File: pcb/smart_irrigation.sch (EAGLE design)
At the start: 22 parts, among them IC1 7805DT, IC2 7833DT, IC3 TMP36, J1 1X2-3.5MM, Q2 32.768

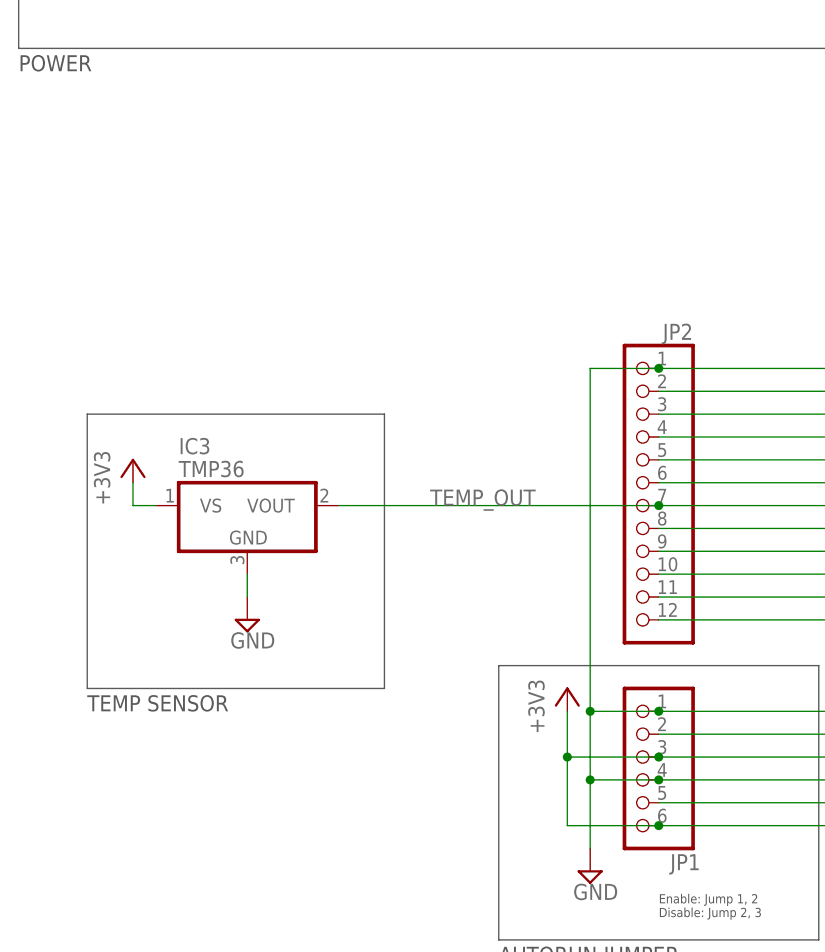
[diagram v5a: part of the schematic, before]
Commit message: PCB: Add soil moisture sensor
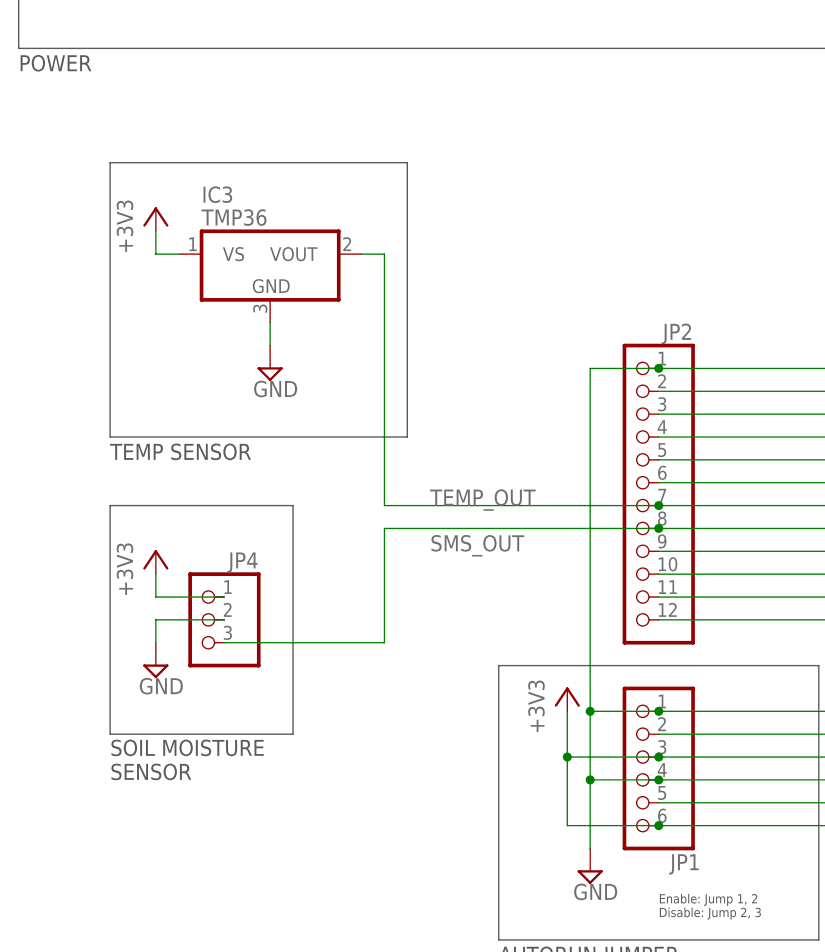
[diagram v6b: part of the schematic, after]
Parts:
- added JP4: (no value), pinhead:PINHD-1X3
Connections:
- removed net N$10: JP2.8, U$1.SIO_2/AIN
- new net SMS_OUT: JP2.8, JP4.3, U$1.SIO_2/AIN
- net +3V3: now also JP4.1
- net GND: now also JP4.2
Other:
- note added: "SOIL MOISTURE SENSOR"
- moved on the sheet: IC3
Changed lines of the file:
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@@
 <part name="+3V5" library="supply1" deviceset="+3V3" device=""/>
 <part name="SUPPLY18" library="supply2" deviceset="GND" device=""/>
+<part name="JP4" library="pinhead" deviceset="PINHD-1X3" device=""/>
+<part name="+3V6" library="supply1" deviceset="+3V3" device=""/>
+<part name="SUPPLY21" library="supply2" deviceset="GND" device=""/>
 </parts>
 <sheets>
@@
 <wire x1="210.82" y1="121.92" x2="210.82" y2="71.12" width="0.1524" layer="97"/>
 <text x="210.82" y="68.58" size="1.778" layer="97">RTC</text>
-<wire x1="12.7" y1="127" x2="45.72" y2="127" width="0.1524" layer="97"/>
-<wire x1="45.72" y1="127" x2="45.72" y2="96.52" width="0.1524" layer="97"/>
-<wire x1="45.72" y1="96.52" x2="12.7" y2="96.52" width="0.1524" layer="97"/>
-<wire x1="12.7" y1="96.52" x2="12.7" y2="127" width="0.1524" layer="97"/>
-<text x="12.7" y="93.98" size="1.778" layer="97">TEMP SENSOR</text>
+<wire x1="15.24" y1="154.94" x2="48.26" y2="154.94" width="0.1524" layer="97"/>
+<wire x1="48.26" y1="154.94" x2="48.26" y2="124.46" width="0.1524" layer="97"/>
+<wire x1="48.26" y1="124.46" x2="15.24" y2="124.46" width="0.1524" layer="97"/>
+<wire x1="15.24" y1="124.46" x2="15.24" y2="154.94" width="0.1524" layer="97"/>
+<text x="15.24" y="121.92" size="1.778" layer="97">TEMP SENSOR</text>
+<wire x1="15.24" y1="116.84" x2="35.56" y2="116.84" width="0.1524" layer="97"/>
+<wire x1="35.56" y1="116.84" x2="35.56" y2="91.44" width="0.1524" layer="97"/>
+<wire x1="35.56" y1="91.44" x2="15.24" y2="91.44" width="0.1524" layer="97"/>
+<wire x1="15.24" y1="91.44" x2="15.24" y2="116.84" width="0.1524" layer="97"/>
+<text x="15.24" y="86.36" size="1.778" layer="97">SOIL MOISTURE
+SENSOR</text>
 </plain>
 <instances>
@@
 <instance part="+3V3" gate="G$1" x="190.5" y="119.38"/>
 <instance part="+3V4" gate="G$1" x="198.12" y="119.38"/>
-<instance part="IC3" gate="A1" x="30.48" y="116.84"/>
-<instance part="+3V5" gate="G$1" x="17.78" y="121.92"/>
-<instance part="SUPPLY18" gate="GND" x="30.48" y="104.14"/>
+<instance part="IC3" gate="A1" x="33.02" y="144.78"/>
+<instance part="+3V5" gate="G$1" x="20.32" y="149.86"/>
+<instance part="SUPPLY18" gate="GND" x="33.02" y="132.08"/>
+<instance part="JP4" gate="A" x="25.4" y="104.14" rot="MR0"/>
+<instance part="+3V6" gate="G$1" x="20.32" y="111.76"/>
+<instance part="SUPPLY21" gate="GND" x="20.32" y="99.06"/>
 </instances>
 <busses>
@@
 <pinref part="IC3" gate="A1" pin="GND"/>
 <pinref part="SUPPLY18" gate="GND" pin="GND"/>
-<wire x1="30.48" y1="109.22" x2="30.48" y2="106.68" width="0.1524" layer="91"/>
+<wire x1="33.02" y1="137.16" x2="33.02" y2="134.62" width="0.1524" layer="91"/>
+</segment>
+<segment>
+<pinref part="SUPPLY21" gate="GND" pin="GND"/>
+<wire x1="20.32" y1="101.6" x2="20.32" y2="104.14" width="0.1524" layer="91"/>
+<pinref part="JP4" gate="A" pin="2"/>
+<wire x1="20.32" y1="104.14" x2="27.94" y2="104.14" width="0.1524" layer="91"/>
 </segment>
 </net>
@@
 <segment>
 <pinref part="+3V5" gate="G$1" pin="+3V3"/>
-<wire x1="17.78" y1="119.38" x2="17.78" y2="116.84" width="0.1524" layer="91"/>
+<wire x1="20.32" y1="147.32" x2="20.32" y2="144.78" width="0.1524" layer="91"/>
 <pinref part="IC3" gate="A1" pin="VS"/>
-<wire x1="17.78" y1="116.84" x2="20.32" y2="116.84" width="0.1524" layer="91"/>
+<wire x1="20.32" y1="144.78" x2="22.86" y2="144.78" width="0.1524" layer="91"/>
+</segment>
+<segment>
+<pinref part="+3V6" gate="G$1" pin="+3V3"/>
+<wire x1="20.32" y1="109.22" x2="20.32" y2="106.68" width="0.1524" layer="91"/>
+<pinref part="JP4" gate="A" pin="1"/>
+<wire x1="20.32" y1="106.68" x2="27.94" y2="106.68" width="0.1524" layer="91"/>
 </segment>
 </net>
@@
 <pinref part="U$1" gate="G$1" pin="SIO_1/AIN"/>
 <wire x1="76.2" y1="116.84" x2="99.06" y2="116.84" width="0.1524" layer="91"/>
+<label x="50.8" y="116.84" size="1.778" layer="95"/>
 <pinref part="IC3" gate="A1" pin="VOUT"/>
-<wire x1="40.64" y1="116.84" x2="76.2" y2="116.84" width="0.1524" layer="91"/>
+<wire x1="43.18" y1="144.78" x2="45.72" y2="144.78" width="0.1524" layer="91"/>
+<wire x1="45.72" y1="144.78" x2="45.72" y2="116.84" width="0.1524" layer="91"/>
+<wire x1="45.72" y1="116.84" x2="76.2" y2="116.84" width="0.1524" layer="91"/>
 <junction x="76.2" y="116.84"/>
-<label x="50.8" y="116.84" size="1.778" layer="95"/>
-</segment>
-</net>
-<net name="N$10" class="0">
+</segment>
+</net>
+<net name="SMS_OUT" class="0">
 <segment>
 <pinref part="U$1" gate="G$1" pin="SIO_2/AIN"/>
 <pinref part="JP2" gate="G$1" pin="8"/>
 <wire x1="99.06" y1="114.3" x2="76.2" y2="114.3" width="0.1524" layer="91"/>
-</segment>
-</net>
+<pinref part="JP4" gate="A" pin="3"/>
+<wire x1="27.94" y1="101.6" x2="45.72" y2="101.6" width="0.1524" layer="91"/>
+<wire x1="45.72" y1="101.6" x2="45.72" y2="114.3" width="0.1524" layer="91"/>
+<wire x1="45.72" y1="114.3" x2="76.2" y2="114.3" width="0.1524" layer="91"/>
+<junction x="76.2" y="114.3"/>
+<label x="50.8" y="111.76" size="1.778" layer="95"/>
+</segment>
+</net>

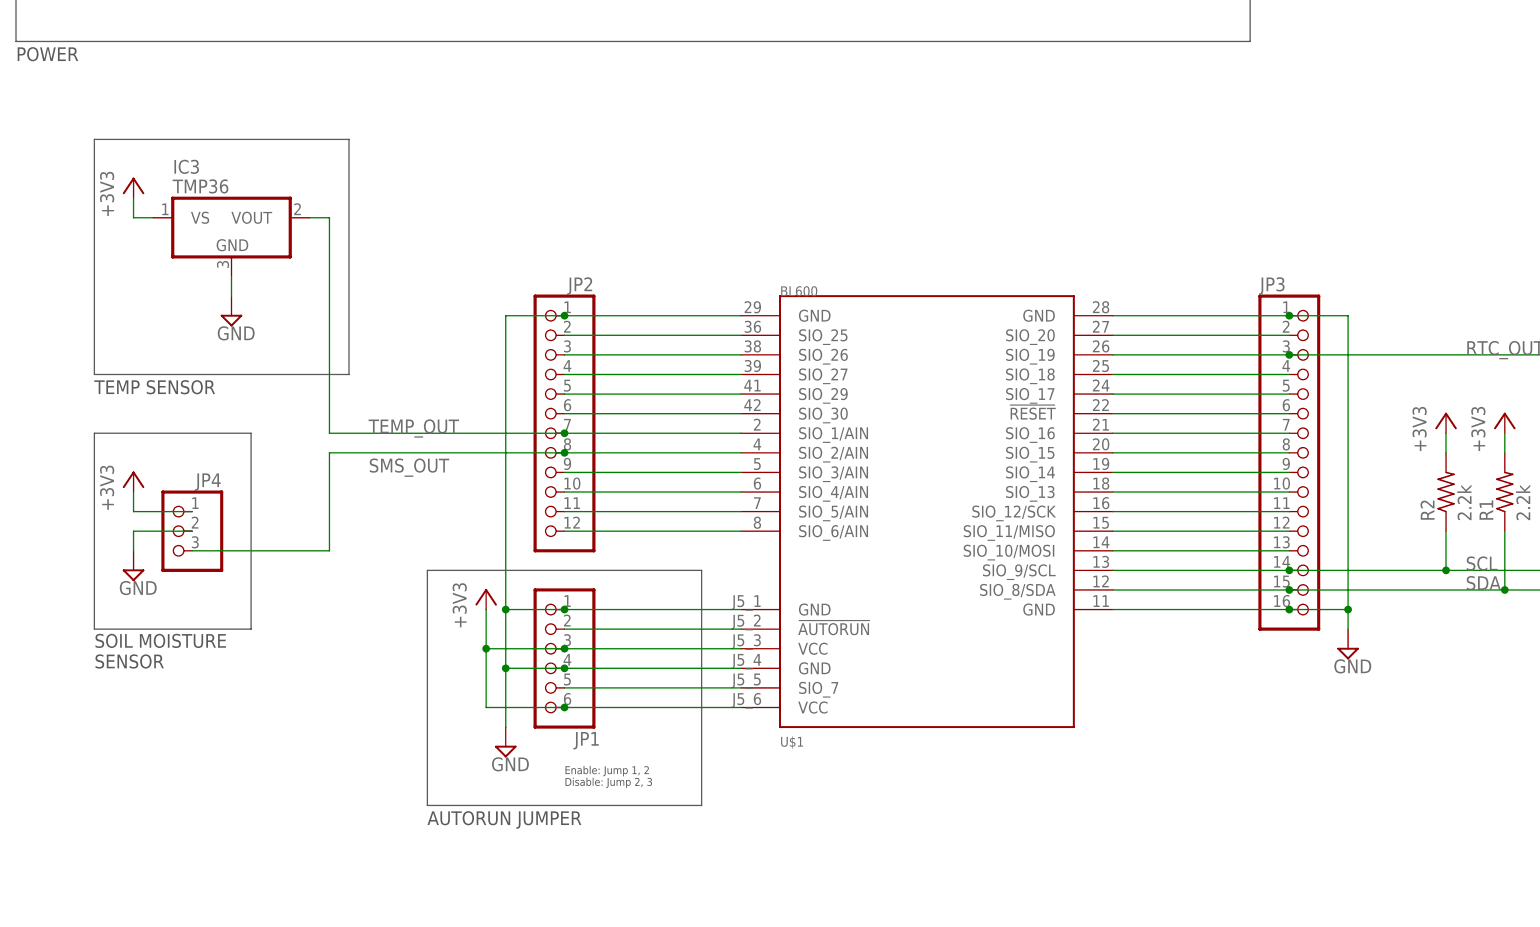
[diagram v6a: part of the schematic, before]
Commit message: PCB: Add raindrop sensor
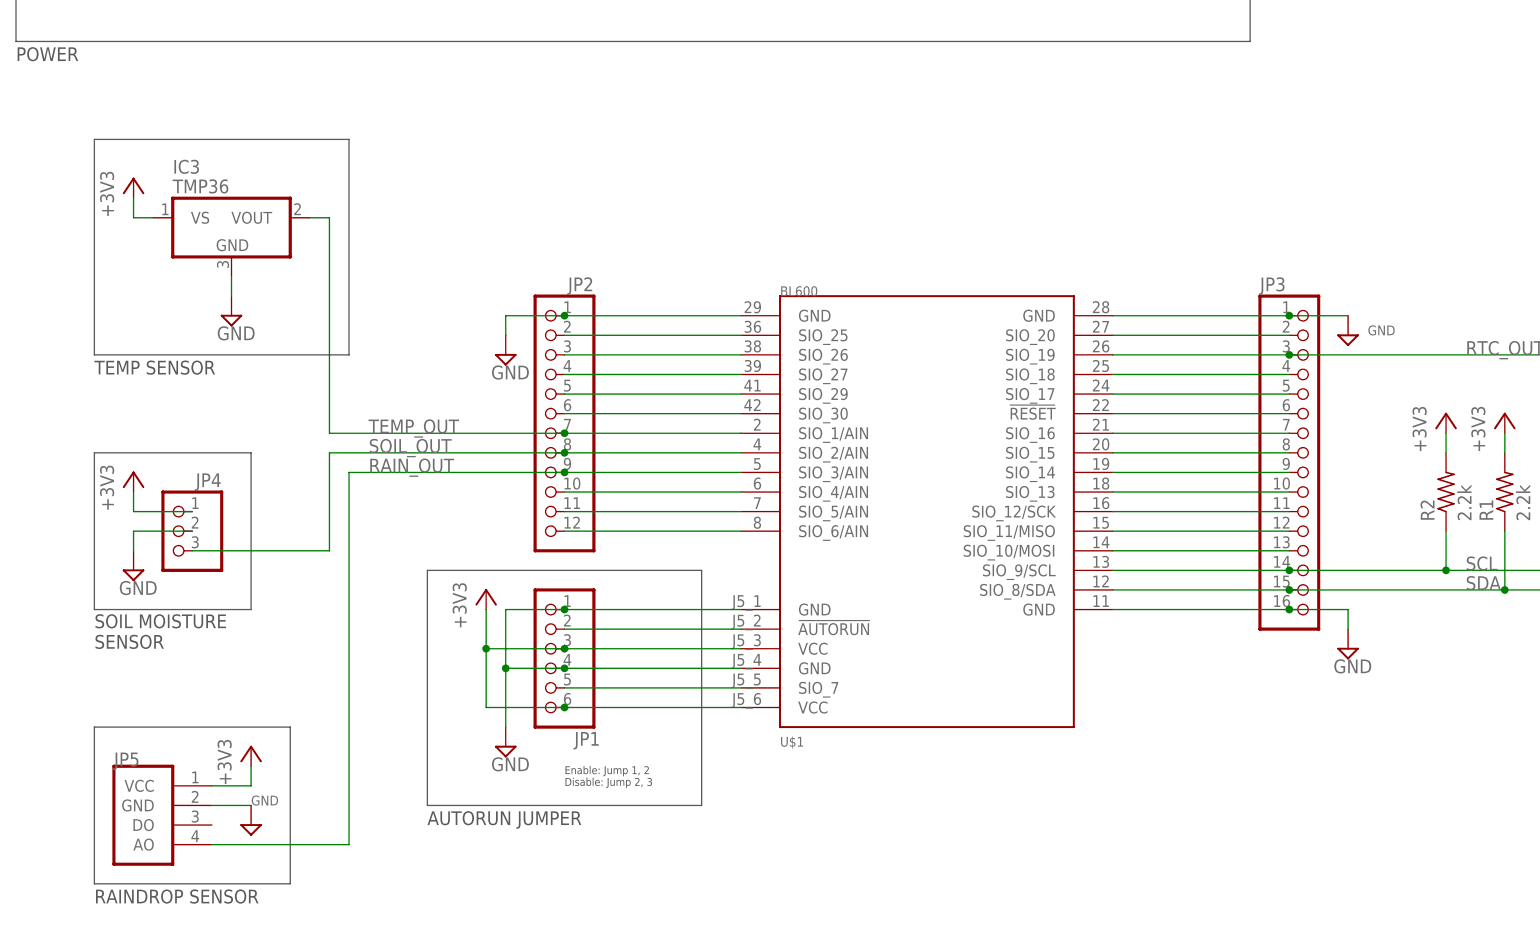
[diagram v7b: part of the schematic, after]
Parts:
- added JP5: (no value), smart_irrigation:RAINDROP
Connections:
- net N$1 renamed NAUTORUN
- net SMS_OUT renamed SOIL_OUT
- removed net N$11: JP2.9, U$1.SIO_3/AIN
- new net RAIN_OUT: JP2.9, JP5.AO, U$1.SIO_3/AIN
- net +3V3: now also JP5.VCC
- net GND: now also JP5.GND
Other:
- note added: "RAINDROP SENSOR"
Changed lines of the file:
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@@
 <part name="+3V6" library="supply1" deviceset="+3V3" device=""/>
 <part name="SUPPLY21" library="supply2" deviceset="GND" device=""/>
+<part name="JP5" library="smart_irrigation" deviceset="RAINDROP" device=""/>
+<part name="+3V7" library="supply1" deviceset="+3V3" device=""/>
+<part name="SUPPLY22" library="supply2" deviceset="GND" device=""/>
+<part name="SUPPLY23" library="supply2" deviceset="GND" device=""/>
+<part name="SUPPLY24" library="supply2" deviceset="GND" device=""/>
 </parts>
 <sheets>
@@
 <text x="210.82" y="68.58" size="1.778" layer="97">RTC</text>
 <wire x1="15.24" y1="154.94" x2="48.26" y2="154.94" width="0.1524" layer="97"/>
-<wire x1="48.26" y1="154.94" x2="48.26" y2="124.46" width="0.1524" layer="97"/>
-<wire x1="48.26" y1="124.46" x2="15.24" y2="124.46" width="0.1524" layer="97"/>
-<wire x1="15.24" y1="124.46" x2="15.24" y2="154.94" width="0.1524" layer="97"/>
-<text x="15.24" y="121.92" size="1.778" layer="97">TEMP SENSOR</text>
-<wire x1="15.24" y1="116.84" x2="35.56" y2="116.84" width="0.1524" layer="97"/>
-<wire x1="35.56" y1="116.84" x2="35.56" y2="91.44" width="0.1524" layer="97"/>
-<wire x1="35.56" y1="91.44" x2="15.24" y2="91.44" width="0.1524" layer="97"/>
-<wire x1="15.24" y1="91.44" x2="15.24" y2="116.84" width="0.1524" layer="97"/>
-<text x="15.24" y="86.36" size="1.778" layer="97">SOIL MOISTURE
+<wire x1="48.26" y1="154.94" x2="48.26" y2="127" width="0.1524" layer="97"/>
+<wire x1="48.26" y1="127" x2="15.24" y2="127" width="0.1524" layer="97"/>
+<wire x1="15.24" y1="127" x2="15.24" y2="154.94" width="0.1524" layer="97"/>
+<text x="15.24" y="124.46" size="1.778" layer="97">TEMP SENSOR</text>
+<wire x1="15.24" y1="114.3" x2="35.56" y2="114.3" width="0.1524" layer="97"/>
+<wire x1="35.56" y1="114.3" x2="35.56" y2="93.98" width="0.1524" layer="97"/>
+<wire x1="35.56" y1="93.98" x2="15.24" y2="93.98" width="0.1524" layer="97"/>
+<wire x1="15.24" y1="93.98" x2="15.24" y2="114.3" width="0.1524" layer="97"/>
+<text x="15.24" y="88.9" size="1.778" layer="97">SOIL MOISTURE
 SENSOR</text>
+<wire x1="15.24" y1="78.74" x2="40.64" y2="78.74" width="0.1524" layer="97"/>
+<wire x1="40.64" y1="78.74" x2="40.64" y2="58.42" width="0.1524" layer="97"/>
+<wire x1="40.64" y1="58.42" x2="15.24" y2="58.42" width="0.1524" layer="97"/>
+<wire x1="15.24" y1="58.42" x2="15.24" y2="78.74" width="0.1524" layer="97"/>
+<text x="15.24" y="55.88" size="1.778" layer="97">RAINDROP SENSOR</text>
 </plain>
 <instances>
@@
 <instance part="+3V6" gate="G$1" x="20.32" y="111.76"/>
 <instance part="SUPPLY21" gate="GND" x="20.32" y="99.06"/>
+<instance part="JP5" gate="A" x="20.32" y="66.04"/>
+<instance part="+3V7" gate="G$1" x="35.56" y="76.2"/>
+<instance part="SUPPLY22" gate="GND" x="35.56" y="66.04" smashed="yes">
+<attribute name="VALUE" x="35.56" y="68.58" size="1.27" layer="96"/>
+</instance>
+<instance part="SUPPLY23" gate="GND" x="68.58" y="127"/>
+<instance part="SUPPLY24" gate="GND" x="177.8" y="129.54" smashed="yes">
+<attribute name="VALUE" x="180.34" y="129.54" size="1.27" layer="96"/>
+</instance>
 </instances>
 <busses>
@@
 <wire x1="99.06" y1="86.36" x2="76.2" y2="86.36" width="0.1524" layer="91"/>
 <junction x="76.2" y="86.36"/>
-<pinref part="U$1" gate="G$1" pin="GND@3"/>
-<pinref part="JP2" gate="G$1" pin="1"/>
-<wire x1="99.06" y1="132.08" x2="76.2" y2="132.08" width="0.1524" layer="91"/>
-<wire x1="68.58" y1="132.08" x2="76.2" y2="132.08" width="0.1524" layer="91"/>
-<junction x="76.2" y="132.08"/>
-<wire x1="68.58" y1="132.08" x2="68.58" y2="93.98" width="0.1524" layer="91"/>
-<junction x="68.58" y="93.98"/>
 </segment>
 <segment>
@@
 <wire x1="177.8" y1="93.98" x2="177.8" y2="91.44" width="0.1524" layer="91"/>
 <junction x="170.18" y="93.98"/>
-<pinref part="U$1" gate="G$1" pin="GND@4"/>
-<pinref part="JP3" gate="A" pin="1"/>
-<wire x1="147.32" y1="132.08" x2="170.18" y2="132.08" width="0.1524" layer="91"/>
-<wire x1="170.18" y1="132.08" x2="177.8" y2="132.08" width="0.1524" layer="91"/>
-<wire x1="177.8" y1="132.08" x2="177.8" y2="93.98" width="0.1524" layer="91"/>
-<junction x="170.18" y="132.08"/>
-<junction x="177.8" y="93.98"/>
 </segment>
 <segment>
@@
 <pinref part="JP4" gate="A" pin="2"/>
 <wire x1="20.32" y1="104.14" x2="27.94" y2="104.14" width="0.1524" layer="91"/>
+</segment>
+<segment>
+<pinref part="JP5" gate="A" pin="GND"/>
+<pinref part="SUPPLY22" gate="GND" pin="GND"/>
+<wire x1="30.48" y1="68.58" x2="35.56" y2="68.58" width="0.1524" layer="91"/>
+</segment>
+<segment>
+<pinref part="JP2" gate="G$1" pin="1"/>
+<pinref part="U$1" gate="G$1" pin="GND@3"/>
+<wire x1="99.06" y1="132.08" x2="76.2" y2="132.08" width="0.1524" layer="91"/>
+<junction x="76.2" y="132.08"/>
+<wire x1="68.58" y1="132.08" x2="76.2" y2="132.08" width="0.1524" layer="91"/>
+<pinref part="SUPPLY23" gate="GND" pin="GND"/>
+<wire x1="68.58" y1="132.08" x2="68.58" y2="129.54" width="0.1524" layer="91"/>
+</segment>
+<segment>
+<pinref part="JP3" gate="A" pin="1"/>
+<wire x1="170.18" y1="132.08" x2="177.8" y2="132.08" width="0.1524" layer="91"/>
+<junction x="170.18" y="132.08"/>
+<pinref part="U$1" gate="G$1" pin="GND@4"/>
+<wire x1="147.32" y1="132.08" x2="170.18" y2="132.08" width="0.1524" layer="91"/>
+<pinref part="SUPPLY24" gate="GND" pin="GND"/>
 </segment>
 </net>
@@
 <wire x1="20.32" y1="106.68" x2="27.94" y2="106.68" width="0.1524" layer="91"/>
 </segment>
-</net>
-<net name="N$1" class="0">
+<segment>
+<pinref part="JP5" gate="A" pin="VCC"/>
+<pinref part="+3V7" gate="G$1" pin="+3V3"/>
+<wire x1="30.48" y1="71.12" x2="35.56" y2="71.12" width="0.1524" layer="91"/>
+<wire x1="35.56" y1="71.12" x2="35.56" y2="73.66" width="0.1524" layer="91"/>
+</segment>
+</net>
+<net name="NAUTORUN" class="0">
 <segment>
 <pinref part="U$1" gate="G$1" pin="!AUTORUN"/>
@@
 </segment>
 </net>
-<net name="SMS_OUT" class="0">
+<net name="SOIL_OUT" class="0">
 <segment>
 <pinref part="U$1" gate="G$1" pin="SIO_2/AIN"/>
@@
 <wire x1="45.72" y1="114.3" x2="76.2" y2="114.3" width="0.1524" layer="91"/>
 <junction x="76.2" y="114.3"/>
-<label x="50.8" y="111.76" size="1.778" layer="95"/>
-</segment>
-</net>
-<net name="N$11" class="0">
+<label x="50.8" y="114.3" size="1.778" layer="95"/>
+</segment>
+</net>
+<net name="RAIN_OUT" class="0">
 <segment>
 <pinref part="JP2" gate="G$1" pin="9"/>
 <pinref part="U$1" gate="G$1" pin="SIO_3/AIN"/>
 <wire x1="76.2" y1="111.76" x2="99.06" y2="111.76" width="0.1524" layer="91"/>
-</segment>
-</net>
+<wire x1="48.26" y1="63.5" x2="48.26" y2="111.76" width="0.1524" layer="91"/>
+<wire x1="48.26" y1="111.76" x2="76.2" y2="111.76" width="0.1524" layer="91"/>
+<junction x="76.2" y="111.76"/>
+<label x="50.8" y="111.76" size="1.778" layer="95"/>
+<pinref part="JP5" gate="A" pin="AO"/>
+<wire x1="30.48" y1="63.5" x2="48.26" y2="63.5" width="0.1524" layer="91"/>
+</segment>
+</net>
